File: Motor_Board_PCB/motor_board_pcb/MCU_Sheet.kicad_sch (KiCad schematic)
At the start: 69 parts, among them J1 CX90B-16P, J2 Barrel_Jack_Switch, J3 TSM-105-01-S-DV-M-TR, J4 Screw_Terminal_01x08, J5 PH2-06-UA, J6 Screw_Terminal_01x04, J7 Screw_Terminal_01x14, SW1 RotaryEncoder_Switch, SW2 SW_Push, U1 R7FA4M1AB3CFM, U2 AP63205WU-7, Y1 16MHz?

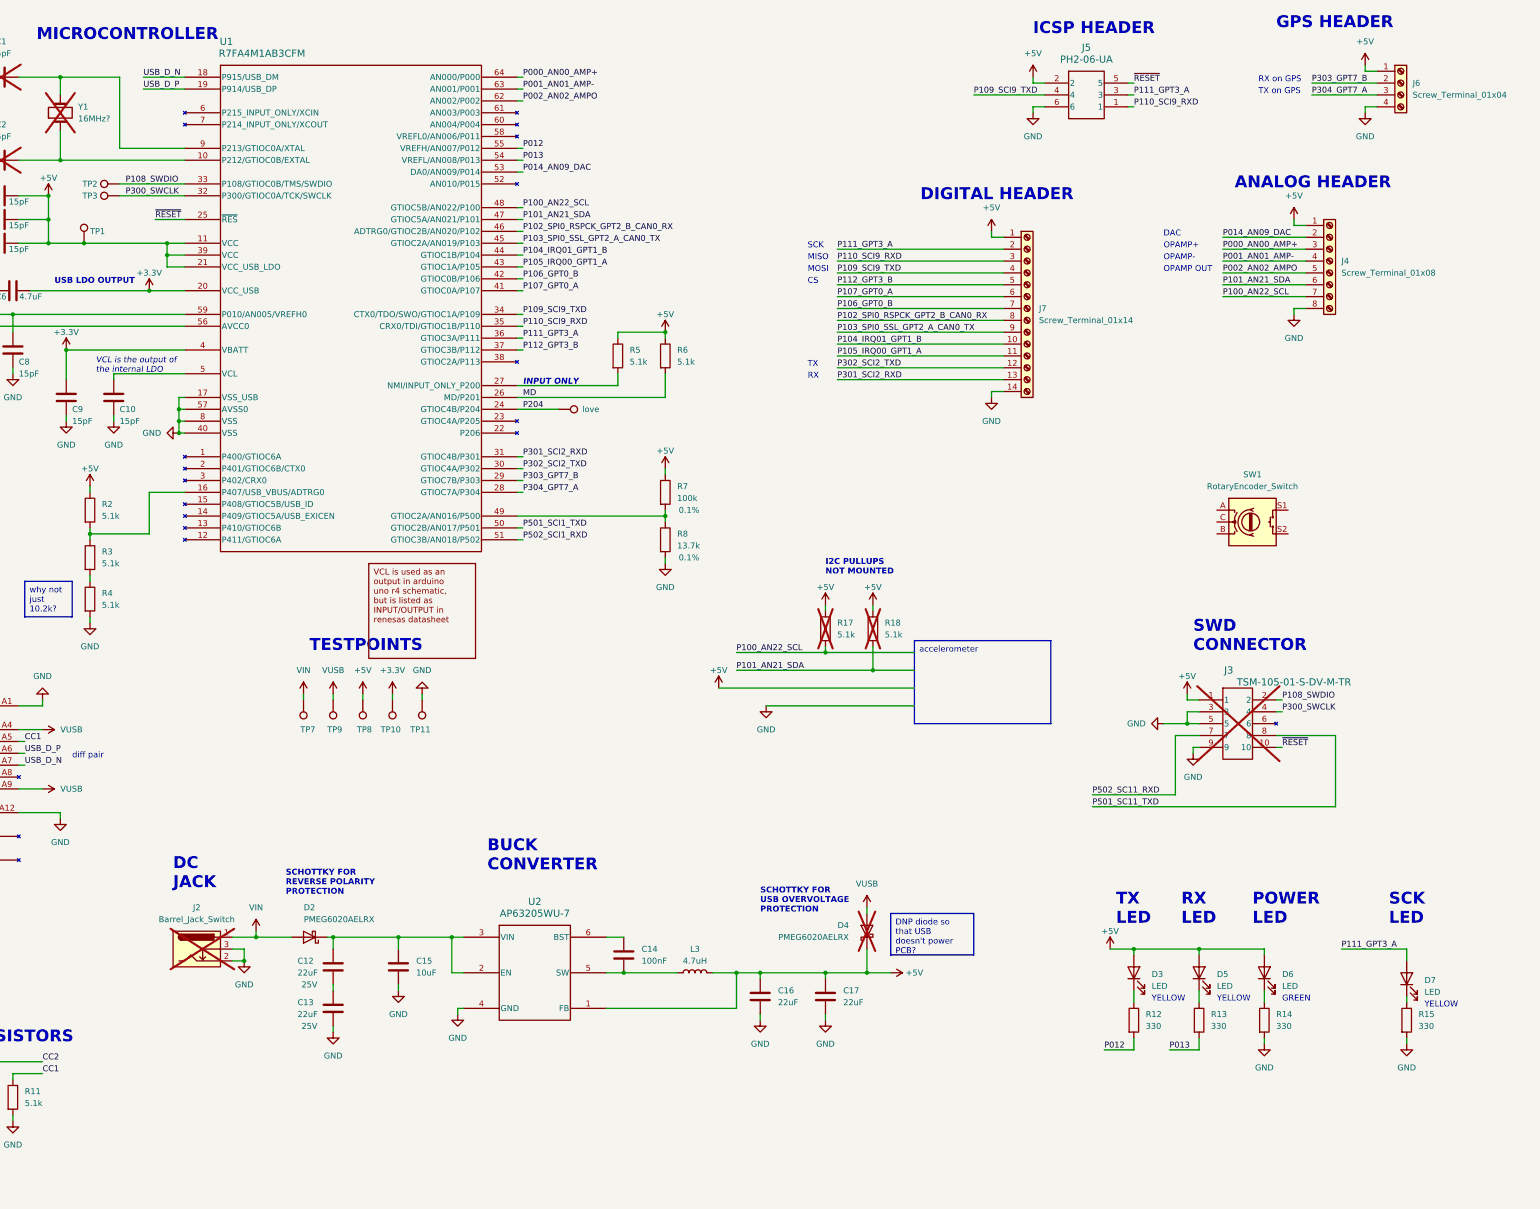
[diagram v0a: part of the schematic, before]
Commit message: Integrated MCU to Motor board
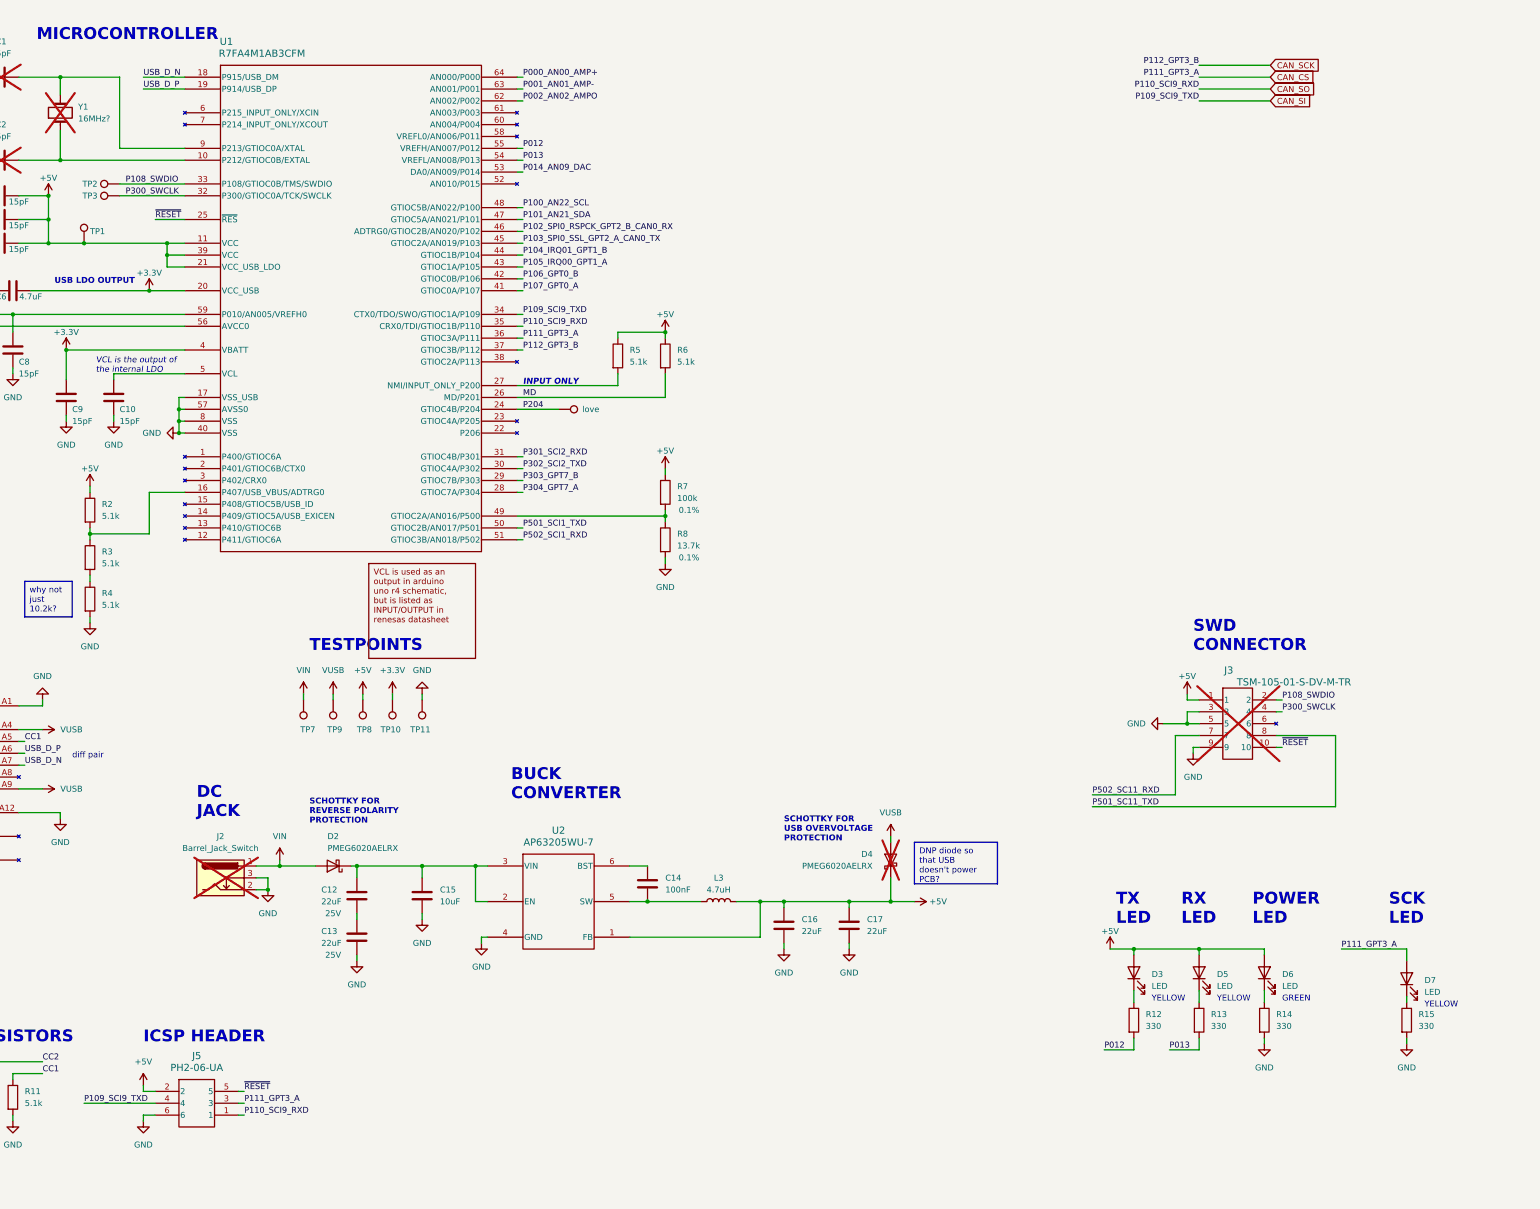
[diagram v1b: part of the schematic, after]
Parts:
- removed J4: Screw_Terminal_01x08, symbol Connector:Screw_Terminal_01x08
- removed J6: Screw_Terminal_01x04, symbol Connector:Screw_Terminal_01x04
- removed J7: Screw_Terminal_01x14, symbol Connector:Screw_Terminal_01x14
- removed R17, R18: 5.1k, symbol Device:R
- removed SW1: RotaryEncoder_Switch, symbol Device:RotaryEncoder_Switch
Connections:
- net P109_SCI9_TXD renamed CAN_SI
- net P110_SCI9_RXD renamed CAN_SO
- net P111_GPT3_A renamed CAN_CS
- net P112_GPT3_B renamed CAN_SCK
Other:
- note removed: "ANALOG HEADER"
- note removed: "CS"
- note removed: "DAC"
- note removed: "DIGITAL HEADER"
- note removed: "GPS HEADER"
- note removed: "I2C PULLUPS NOT MOUNTED"
- note removed: "MISO"
- note removed: "MOSI"
- note removed: "OPAMP OUT"
- note removed: "OPAMP+"
- note removed: "OPAMP-"
- note removed: "RX"
- note removed: "RX on GPS"
- note removed: "SCK"
- note removed: "TX"
- note removed: "TX on GPS"
- moved on the sheet: C12, C13, C14, C15, C16, C17, D2, D4, J2, J5, L3, U2

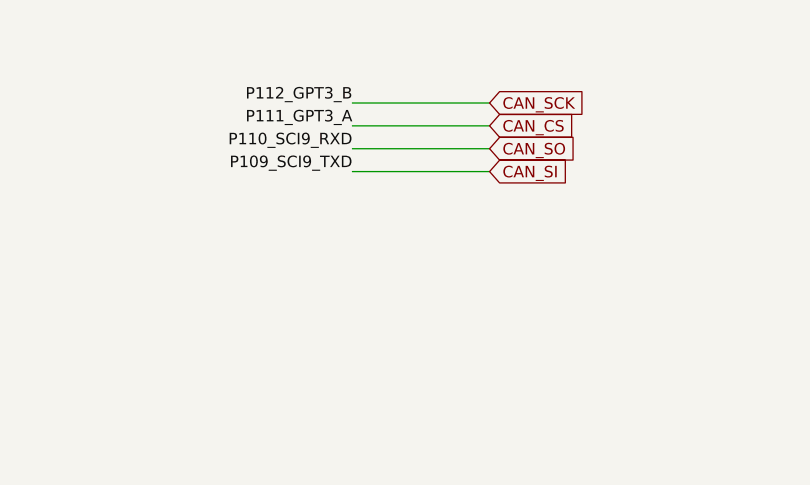
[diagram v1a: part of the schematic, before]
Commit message: Added power and motor driver chip schematics
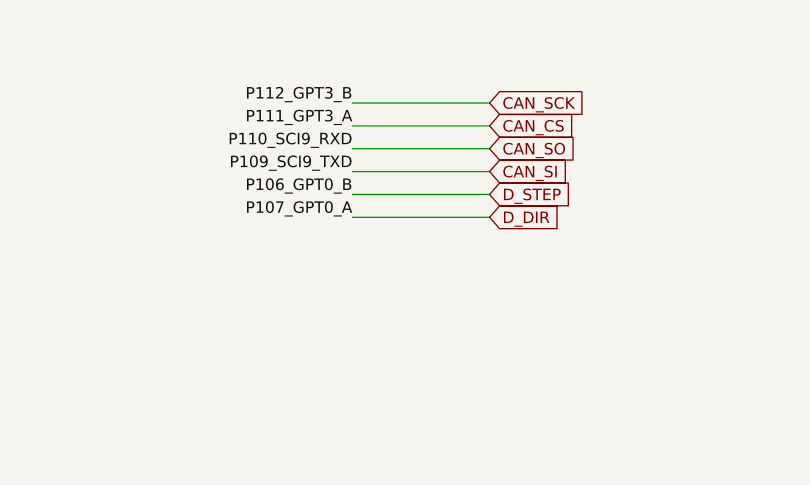
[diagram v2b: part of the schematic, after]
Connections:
- net P106_GPT0_B renamed D_STEP
- net P107_GPT0_A renamed D_DIR
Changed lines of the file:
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@@
+    (stroke (width 0) (type default))
+  )
+  (wire (pts (xy 336.55 39.37) (xy 351.79 39.37))
     (stroke (width 0) (type default))
   )
@@
   )
   (wire (pts (xy 242.57 215.9) (xy 242.57 208.28))
+    (stroke (width 0) (type default))
+  )
+  (wire (pts (xy 336.55 41.91) (xy 351.79 41.91))
     (stroke (width 0) (type default))
   )
@@
     (effects (font (size 1.27 1.27)) (justify left bottom))
   )
+  (label "P106_GPT0_B" (at 336.55 39.37 180) (fields_autoplaced)
+    (effects (font (size 1.27 1.27)) (justify right bottom))
+  )
   (label "P104_IRQ01_GPT1_B" (at 191.77 69.85 0) (fields_autoplaced)
     (effects (font (size 1.27 1.27)) (justify left bottom))
@@
   (label "P105_IRQ00_GPT1_A" (at 191.77 72.39 0) (fields_autoplaced)
     (effects (font (size 1.27 1.27)) (justify left bottom))
+  )
+  (label "P107_GPT0_A" (at 336.55 41.91 180) (fields_autoplaced)
+    (effects (font (size 1.27 1.27)) (justify right bottom))
   )
   (label "AREF" (at 25.4 76.2 0) (fields_autoplaced)
@@
     )
   )
+  (global_label "D_STEP" (shape input) (at 351.79 39.37 0) (fields_autoplaced)
+    (effects (font (size 1.27 1.27)) (justify left))
+    (property "Intersheetrefs" "${INTERSHEET_REFS}" (at 361.6089 39.37 0)
+      (effects (font (size 1.27 1.27)) (justify left) hide)
+    )
+  )
   (global_label "CAN_SO" (shape input) (at 351.79 34.29 0) (fields_autoplaced)
     (effects (font (size 1.27 1.27)) (justify left))
@@
       (effects (font (size 1.27 1.27)) (justify left) hide)
     )
+  )
+  (global_label "D_DIR" (shape input) (at 351.79 41.91 0) (fields_autoplaced)
+    (effects (font (size 1.27 1.27)) (justify left))
+    (property "Intersheetrefs" "${INTERSHEET_REFS}" (at 360.1576 41.91 0)
+      (effects (font (size 1.27 1.27)) (justify left) hide)
+    )
